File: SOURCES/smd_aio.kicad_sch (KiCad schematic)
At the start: 64 parts, among them J1 RCA_01, J2 RCA_01, P1 CONN_01X06, P16 TST, P2 CONN_01X04, P23 TST, P3 CONN_01X03, P4 CONN_02X05 Boxed, P5 STDCONN, P6 CONN_02X04, P7 CONN_02X04, P8 CONN_02X04, Q1 BSS123, Q2 BSS123, Q3 BSS123, Q4 BSS123, Q5 FZT751TA, SW1 SW_PUSH, U1 ADAU1701, U2 24AA256SN

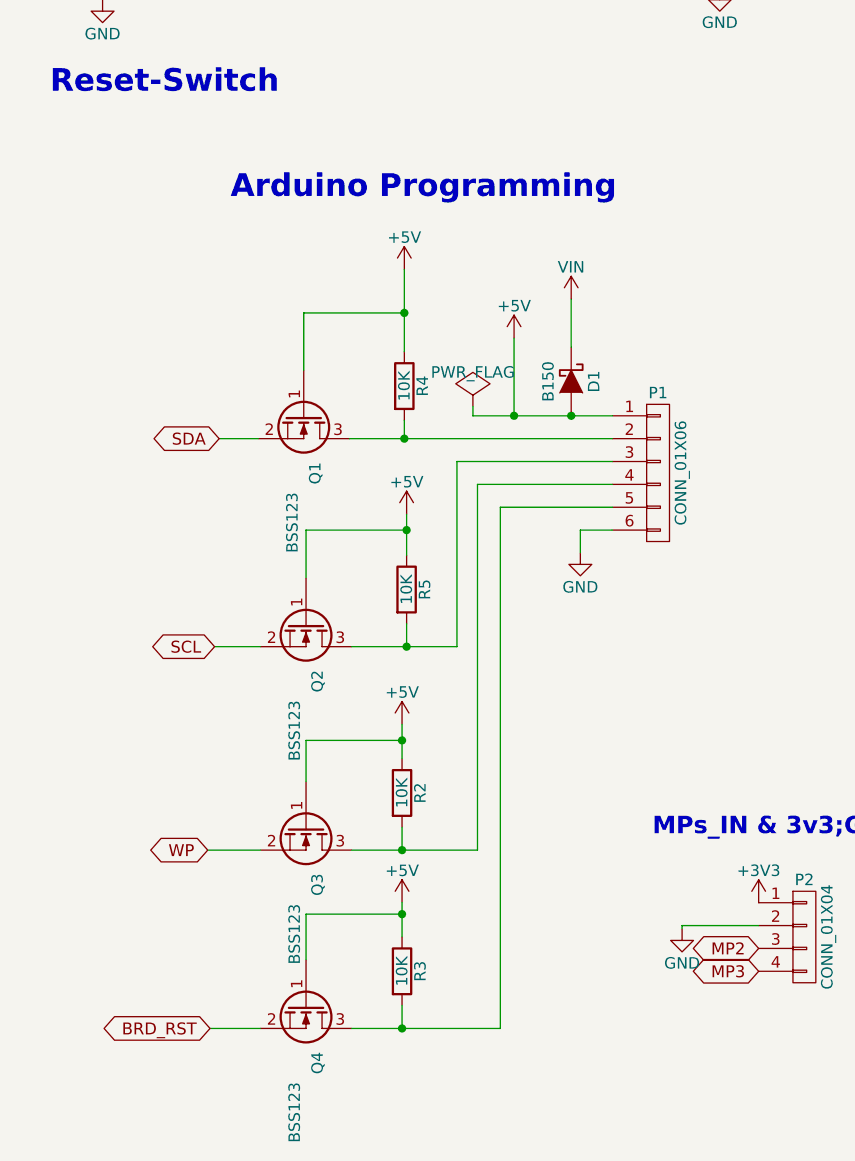
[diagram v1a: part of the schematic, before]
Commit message: Removed redundant 7414 and pot, rerouted a bit.
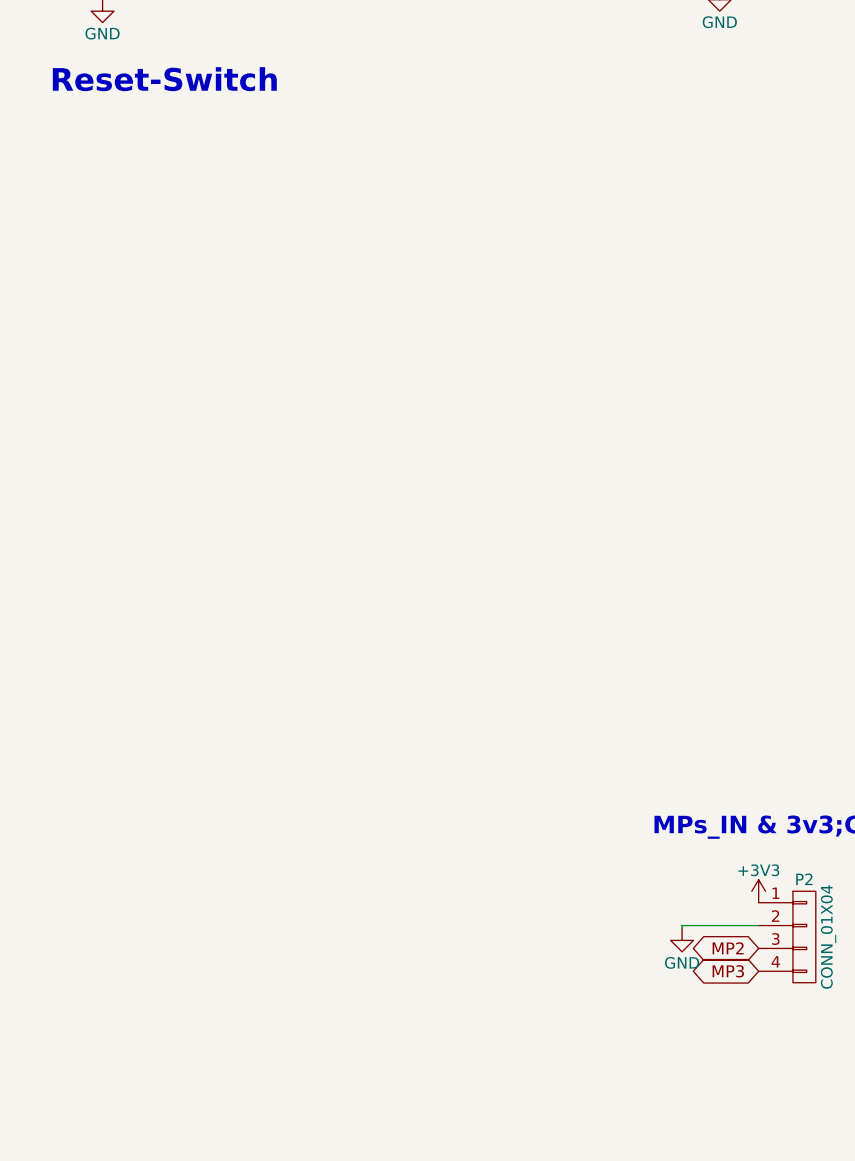
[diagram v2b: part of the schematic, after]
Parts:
- removed D1: B150, fdsp_diode:SMA, symbol smd_aio-rescue:D_Schottky
- removed P1: CONN_01X06, fdsp_pinheader:Pin_Header_Straight_1x06, symbol smd_aio-rescue:CONN_01X06
- removed Q1, Q2, Q3, Q4: BSS123, fdsp_housing_new:SOT-23_Handsoldering, symbol smd_aio-rescue:NMOS_GSD
- removed R2, R3, R4, R5: 10K, fdsp_resistor:R_1206_HandSoldering, symbol smd_aio-rescue:R
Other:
- note removed: "Arduino Programming"

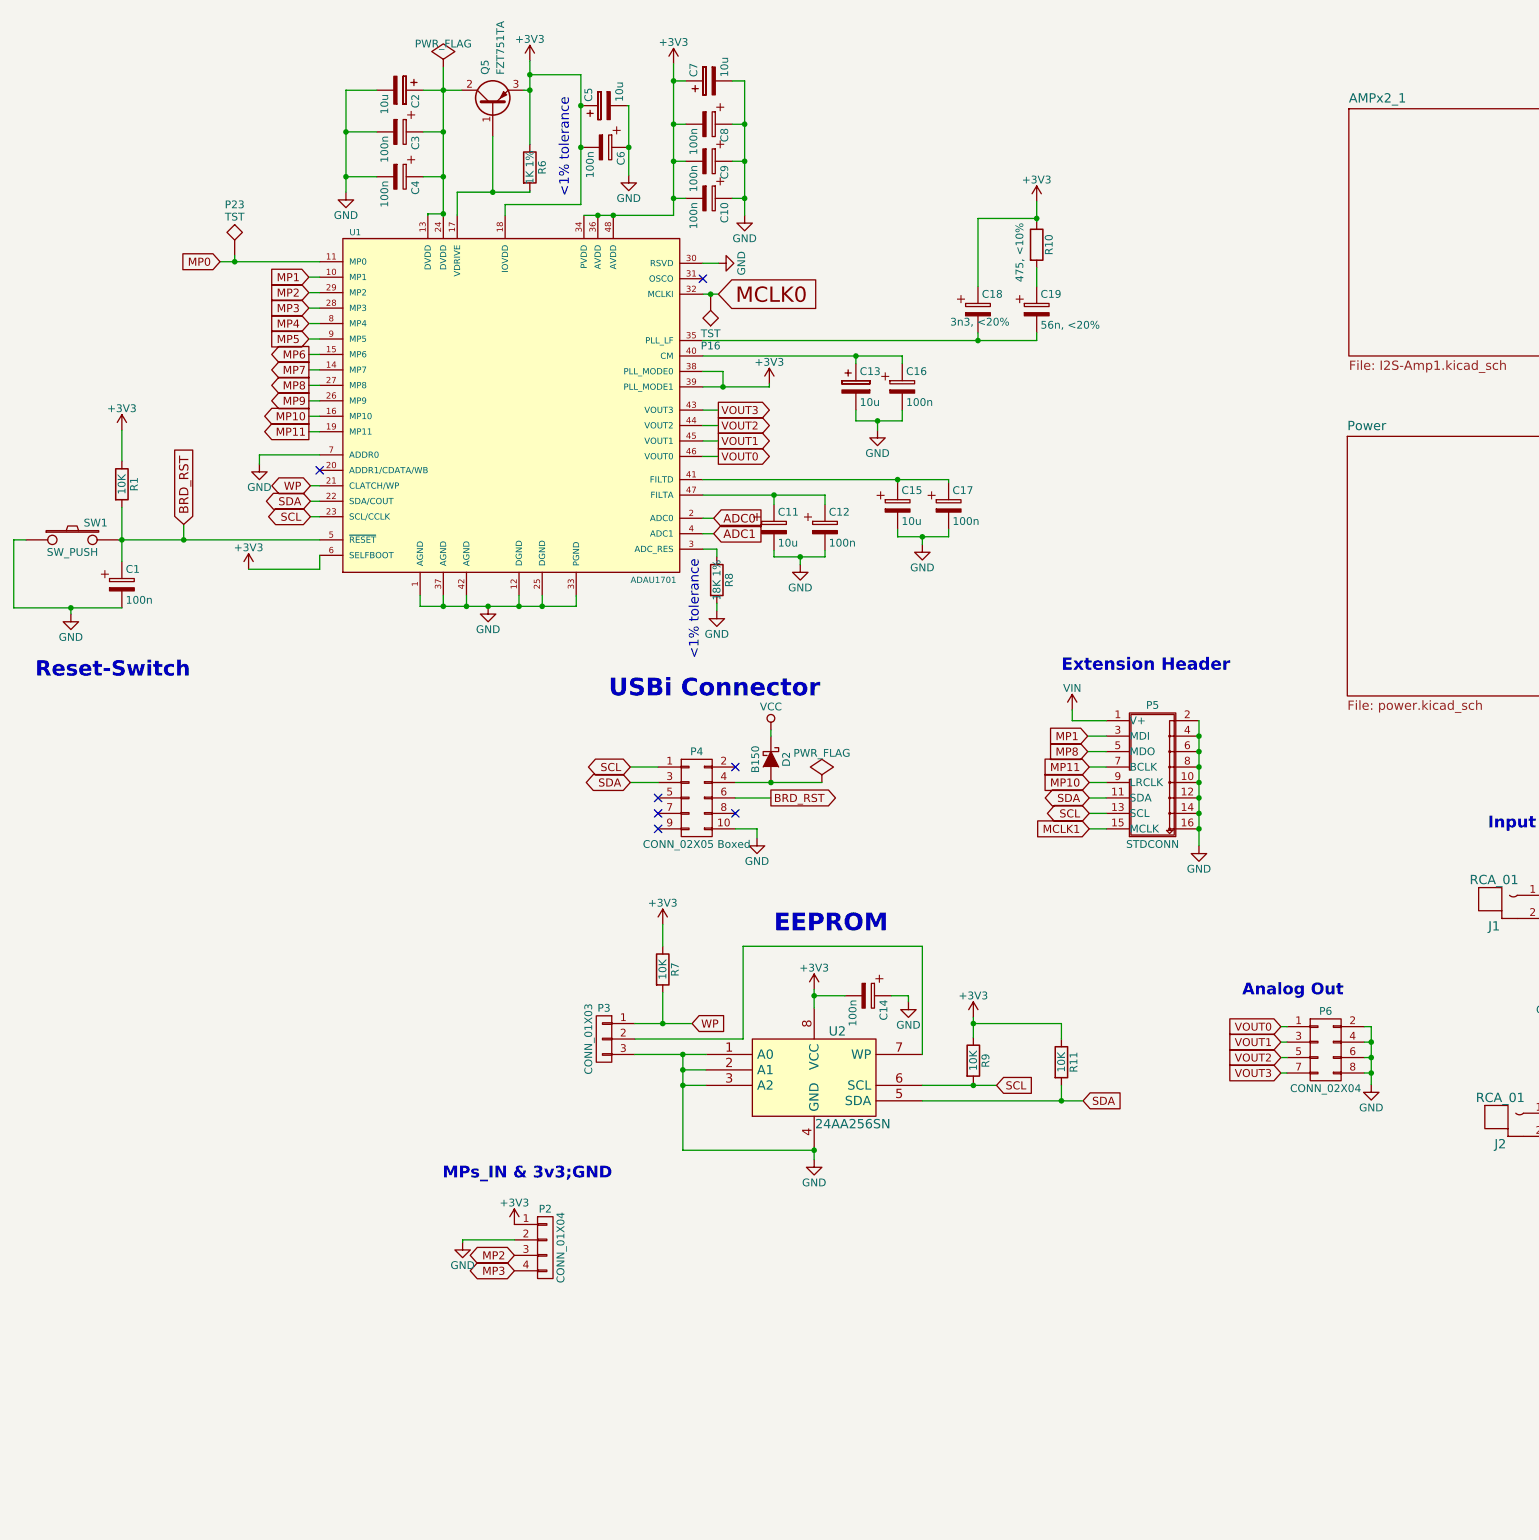
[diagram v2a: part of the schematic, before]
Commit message: Removed ArduinoPort, Changed Power Supply. Rerouting and stuff.
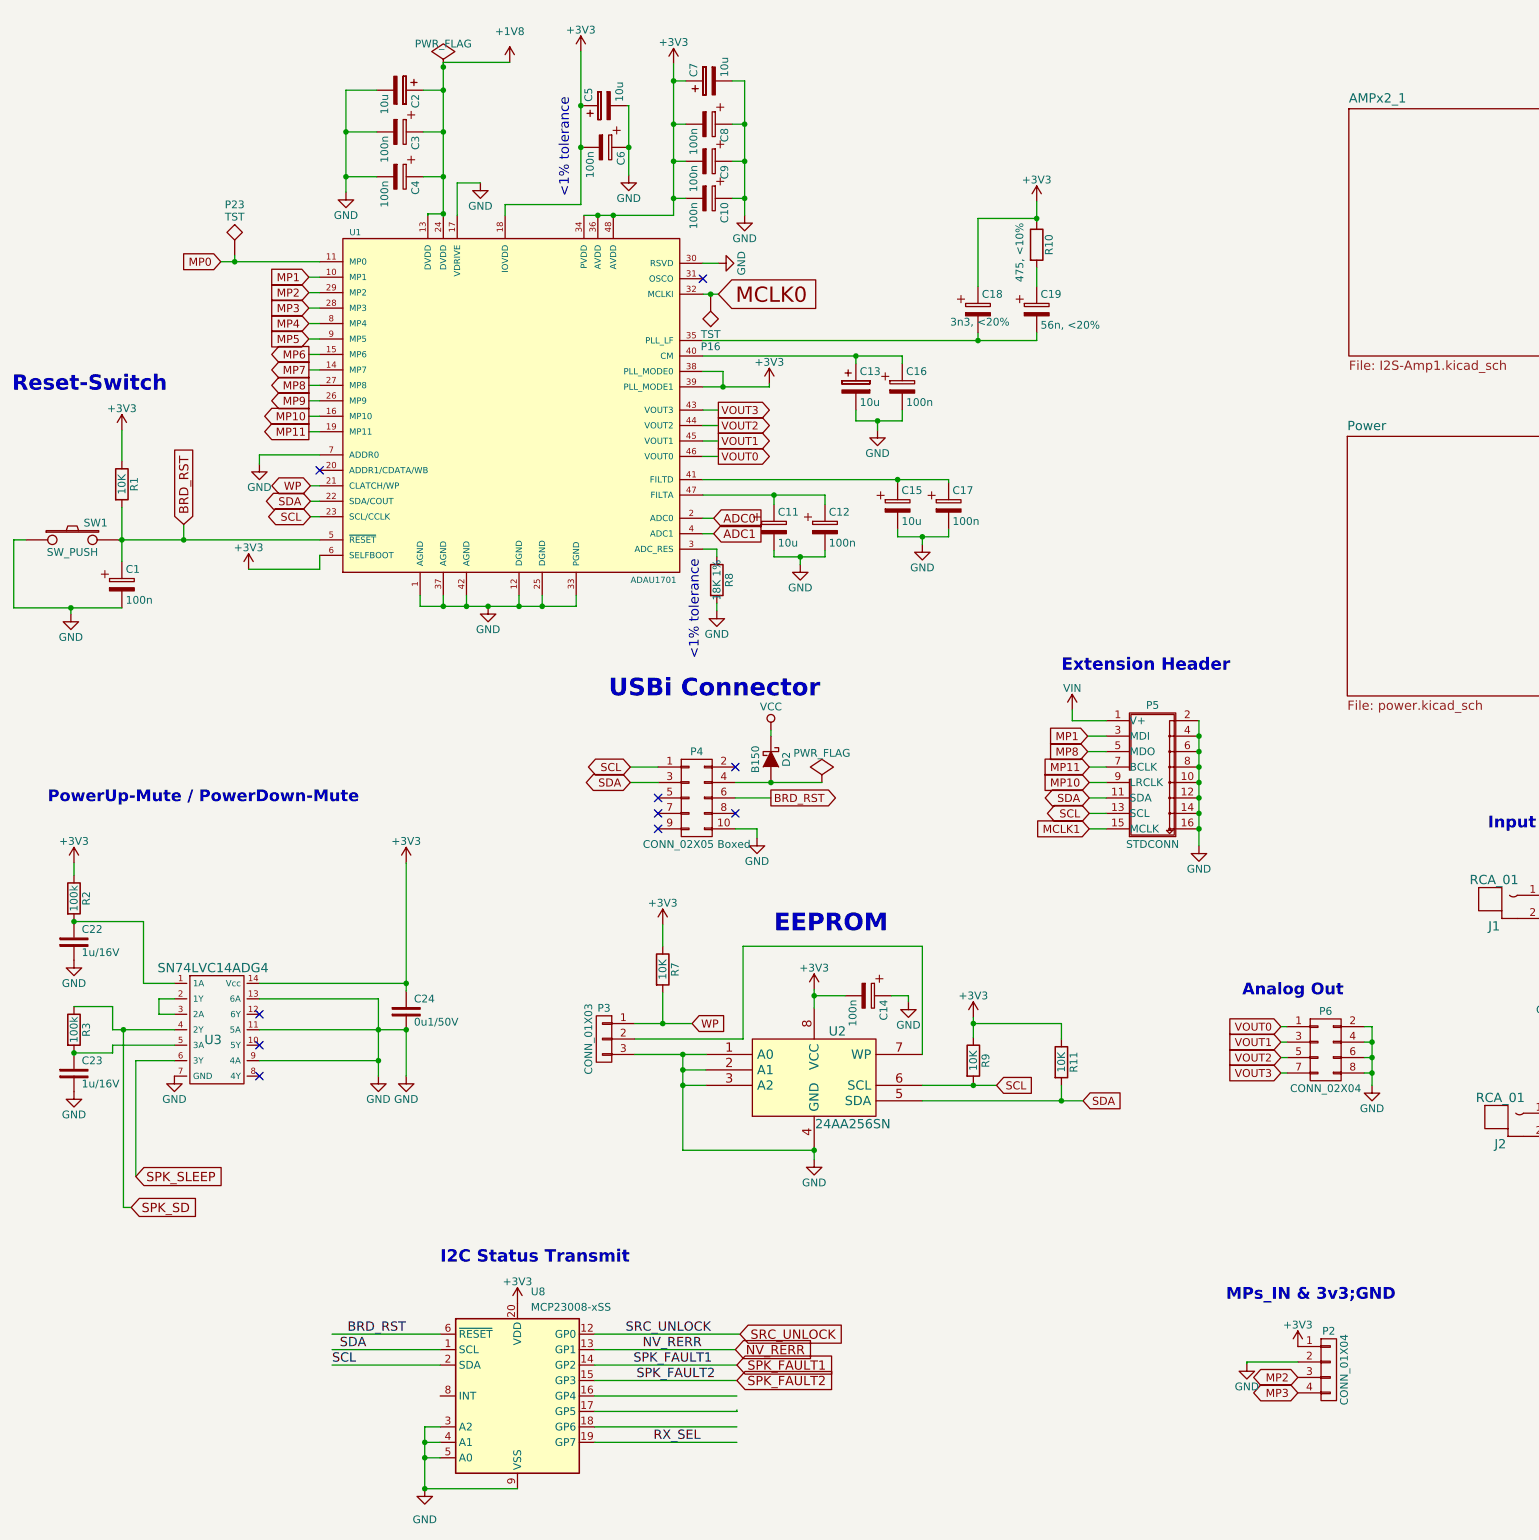
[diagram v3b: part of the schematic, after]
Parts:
- removed Q5: FZT751TA, fdsp_housing_new:SOT-223, symbol smd_aio-rescue:Q_PNP_BCE
- removed R6: 1K 1%, fdsp_resistor:R_1206_HandSoldering, symbol smd_aio-rescue:R
- added C22, C23: 1u/16V, fdsp_capacitor:C_1206_HandSoldering, symbol MyLibrary:Capacitor
- added C24: 0u1/50V, fdsp_capacitor:C_1206_HandSoldering, symbol MyLibrary:Capacitor
- added R2, R3: 100k, fdsp_resistor:R_1206_HandSoldering, symbol smd_aio-rescue:R
- added U3: SN74LVC14ADG4, Housings_SOIC:SOIC-14_3.9x8.7mm_Pitch1.27mm, symbol MyLibrary:SN74LVC14ADG4
- added U8: MCP23008-xSS, Package_SO:SSOP-20_5.3x7.2mm_P0.65mm, symbol Interface_Expansion:MCP23008-xSS
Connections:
- net +3V3: now also C24.1, R2.1, U3.14 (Vcc), U8.20 (VDD)
- net BRD_RST: now also U8.6 (~{RESET})
- net GND: now also U1.17 (VDRIVE), C22.2, C23.2, C24.2, U3.11 (5A), U3.13 (6A), U3.7 (GND), U3.9 (4A), U8.3 (A2), U8.4 (A1), U8.5 (A0), U8.9 (VSS)
- net SCL: now also U8.2 (SDA)
- net SDA: now also U8.1 (SCL)
- net +1V8: now reaches C2.1, C3.1, C4.1, U1.13 (DVDD), U1.24 (DVDD)
- new net: C22.1, R2.2, U3.1 (1A)
- new net: U3.2 (1Y), U3.3 (2A)
- new net: C23.1, R3.2, U3.5 (3A)
- new net NV_RERR: U8.13 (GP1)
- new net RX_SEL: U8.19 (GP7)
- new net SPK_FAULT1: U8.14 (GP2)
- new net SPK_FAULT2: U8.15 (GP3)
- new net SPK_SD: R3.1, U3.4 (2Y)
- new net SPK_SLEEP: U3.6 (3Y)
- new net SRC_UNLOCK: U8.12 (GP0)
- no-connect marks 7 -> 10
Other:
- note added: "I2C Status Transmit"
- note added: "PowerUp-Mute / PowerDown-Mute"
- moved on the sheet: P2

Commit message: Added power down detection.
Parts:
- added D1, D11: B150, fdsp_diode:SMA, symbol smd_aio-rescue:D_Schottky
- added P1: MUTE, fdsp_misc:Measurement_Point_Round-SMD-Pad_Small, symbol smd_aio-rescue:TST
- added P32: /SD, fdsp_misc:Measurement_Point_Round-SMD-Pad_Small, symbol smd_aio-rescue:TST
- added P33: GP4, fdsp_misc:Measurement_Point_Round-SMD-Pad_Small, symbol smd_aio-rescue:TST
- added P34: GP5, fdsp_misc:Measurement_Point_Round-SMD-Pad_Small, symbol smd_aio-rescue:TST
- added P35: GP6, fdsp_misc:Measurement_Point_Round-SMD-Pad_Small, symbol smd_aio-rescue:TST
- added R4, R5: 10K, fdsp_resistor:R_1206_HandSoldering, symbol smd_aio-rescue:R
- added RV2: 100k, AMPx2 _footprints:M64Z104KB40, symbol smd_aio-rescue:POT
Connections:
- net GND: now also R4.2; no longer U3.9 (4A)
- net SPK_SD: now also P32.1
- net SPK_SLEEP: now also D1.1 (K), D11.1 (K), P1.1; no longer U3.6 (3Y)
- net VCC: now also RV2.3
- net at U3.8 (4Y): now also D11.2 (A)
- net at U8.16 (GP4): now also P33.1
- net at U8.17 (GP5): now also P34.1
- net at U8.18 (GP6): now also P35.1
- new net: D1.2 (A), U3.6 (3Y)
- new net: R5.1, U3.9 (4A)
- new net: R4.1, RV2.1
- new net: R5.2, RV2.2
- no-connect marks 10 -> 9
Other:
- note added: "<< Adjust shut down voltage <<"
- note added: "MUTE"
- note added: "SHUT DOWN"
- moved on the sheet: C22, C23, R2, R3

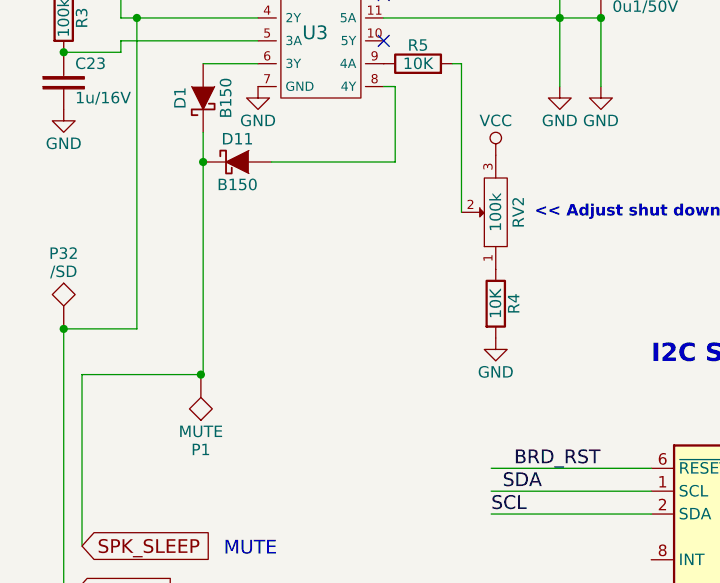
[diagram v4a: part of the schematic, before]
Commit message: Moved input cap and Reset btn.
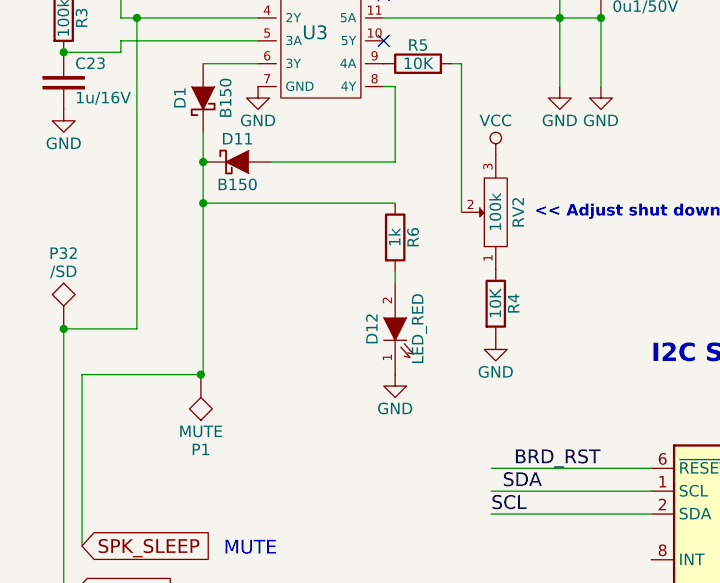
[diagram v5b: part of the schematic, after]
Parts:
- added D12: LED_RED, fdsp_resistor:R_1206_HandSoldering, symbol smd_aio-rescue:LED
- added R6: 1k, fdsp_resistor:R_1206_HandSoldering, symbol smd_aio-rescue:R
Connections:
- net GND: now also D12.1 (K)
- net SPK_SLEEP: now also R6.1
- new net: D12.2 (A), R6.2
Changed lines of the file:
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@@
   (junction (at 276.098 162.814) (diameter 0) (color 0 0 0 0)
   )
+  (junction (at 39.116 205.486) (diameter 0) (color 0 0 0 0)
+  )
   (junction (at 330.454 203.708) (diameter 0) (color 0 0 0 0)
   )
@@
   (no_connect (at 59.182 187.452))
   (no_connect (at 124.714 149.352))
+  (wire (pts (xy 60.452 213.106) (xy 60.452 214.376))
+    (stroke (width 0) (type default))
+  )
   (wire (pts (xy 91.694 45.72) (xy 95.504 45.72))
     (stroke (width 0) (type default))
@@
     (stroke (width 0) (type default))
   )
-  (wire (pts (xy 39.116 224.536) (xy 39.116 200.914))
+  (wire (pts (xy 39.116 224.536) (xy 39.116 205.486))
     (stroke (width 0) (type default))
   )
@@
     (stroke (width 0) (type default))
   )
+  (wire (pts (xy 39.116 205.486) (xy 60.452 205.486))
+    (stroke (width 0) (type default))
+  )
   (wire (pts (xy 327.152 170.434) (xy 329.438 170.434))
     (stroke (width 0) (type default))
@@
     (stroke (width 0) (type default))
   )
+  (wire (pts (xy 39.116 205.486) (xy 39.116 200.914))
+    (stroke (width 0) (type default))
+  )
   (wire (pts (xy 277.114 198.628) (xy 281.178 198.628))
     (stroke (width 0) (type default))
@@
     )
   )
+  (symbol (lib_id "smd_aio-rescue:R") (at 60.452 209.296 0) (unit 1)
+    (in_bom yes) (on_board yes) (dnp no)
+    (property "Reference" "R6" (at 62.484 209.296 90)
+      (effects (font (size 1.27 1.27)))
+    )
+    (property "Value" "1k" (at 60.452 209.296 90)
+      (effects (font (size 1.27 1.27)))
+    )
+    (property "Footprint" "fdsp_resistor:R_1206_HandSoldering" (at 58.674 209.296 90)
+      (effects (font (size 0.762 0.762)) hide)
+    )
+    (property "Datasheet" "" (at 60.452 209.296 0)
+      (effects (font (size 0.762 0.762)))
+    )
+    (pin "1")
+    (pin "2")
+    (instances
+      (project "smd_aio"
+        (path "/4c49a07c-9ad4-4758-901a-e68e360dc17d"
+          (reference "R6") (unit 1)
+        )
+      )
+    )
+  )
   (symbol (lib_id "MyLibrary:SN74LVC14ADG4") (at 54.102 186.182 0) (unit 1)
     (in_bom yes) (on_board yes) (dnp no)
@@
     )
   )
+  (symbol (lib_id "smd_aio-rescue:GND") (at 60.452 224.536 0) (unit 1)
+    (in_bom yes) (on_board yes) (dnp no)
+    (property "Reference" "#PWR0107" (at 60.452 230.886 0)
+      (effects (font (size 1.27 1.27)) hide)
+    )
+    (property "Value" "GND" (at 60.452 228.346 0)
+      (effects (font (size 1.27 1.27)))
+    )
+    (property "Footprint" "" (at 60.452 224.536 0)
+      (effects (font (size 1.27 1.27)))
+    )
+    (property "Datasheet" "" (at 60.452 224.536 0)
+      (effects (font (size 1.27 1.27)))
+    )
+    (pin "1")
+    (instances
+      (project "smd_aio"
+        (path "/4c49a07c-9ad4-4758-901a-e68e360dc17d"
+          (reference "#PWR0107") (unit 1)
+        )
+      )
+    )
+  )
   (symbol (lib_id "smd_aio-rescue:GND") (at 71.628 220.472 0) (unit 1)
     (in_bom yes) (on_board yes) (dnp no)
@@
         )
       )
+    )
+  )
+  (symbol (lib_id "smd_aio-rescue:LED") (at 60.452 219.456 90) (unit 1)
+    (in_bom yes) (on_board yes) (dnp no)
+    (property "Reference" "D12" (at 57.912 219.456 0)
+      (effects (font (size 1.27 1.27)))
+    )
+    (property "Value" "LED_RED" (at 62.992 219.456 0)
+      (effects (font (size 1.27 1.27)))
+    )
+    (property "Footprint" "fdsp_resistor:R_1206_HandSoldering" (at 60.452 219.456 0)
+      (effects (font (size 1.524 1.524)) hide)
+    )
+    (property "Datasheet" "" (at 60.452 219.456 0)
+      (effects (font (size 1.524 1.524)))
+    )
+    (pin "1")
+    (pin "2")
+    (instances
+      (project "smd_aio"
+        (path "/4c49a07c-9ad4-4758-901a-e68e360dc17d"
+          (reference "D12") (unit 1)
+        )
+      )
